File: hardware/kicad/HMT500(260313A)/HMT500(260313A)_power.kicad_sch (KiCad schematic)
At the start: 21 parts, among them U1 TPS26600PWPR, U2 LMR36006, U3 TPS7A2033PDBVR

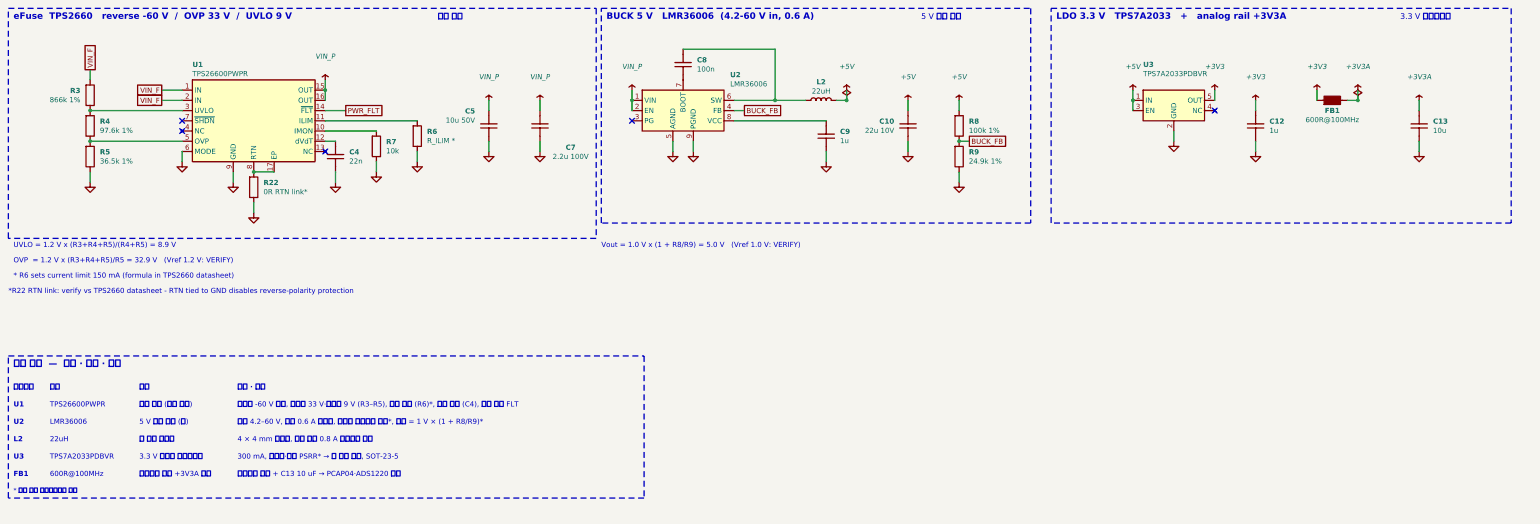
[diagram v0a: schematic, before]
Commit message: Schematic v0.8: apply datasheet review A-O (HMT500(260313A))
- Real pinouts from manufacturer datasheets: LMR36006BRNXR (RNX-12),
  TPS26611DDFR (SOT-23-8), PCAP04 (QFN24); TPS2660 PowerPAD = RTN
- TPS2660: RTN isolated from GND (R22, R7 removed); R5/R6/C4/MODE on
  EF_RTN; R6 80.6k (149 mA); R5 41.2k -> OVP 29 V, supply 12-28 V so
  TPS26611 +Vs stays <= 30 V
- DAC SPI: per-DAC SCLK gating (74LVC2G32, SPI2 mode 3, LATCH1/2 on
  PB10/PB11) - daisy chain was removed in DAC8760 rev D
- DAC AVDD 10R series, ALARM wired-OR with 10k pull-up (PB6)
- Output TVS -> TVS3301 (stacked-pin two-terminal symbol)
- PCAP04 on dedicated SPI3 (PB3/4/5), VDD18 4.7uF, VDD33 10uF
- Buck per datasheet: L 15uH, COUT 2x22uF, CFF 20pF
- Shared VIN_P bulk (C53, C26 removed); PWR_FLT PB7; SGOOD -> PC6/PC7
- Parts list, circuit-design, decision log #26, review doc updated;
  netlist 74/74, 0 errors; tests pass

Co-Authored-By: Claude Opus 5.5 <noreply@anthropic.com>
Claude-Session: https://claude.ai/code/session_01JA2o8uJsqp9Vzsg4b665ev
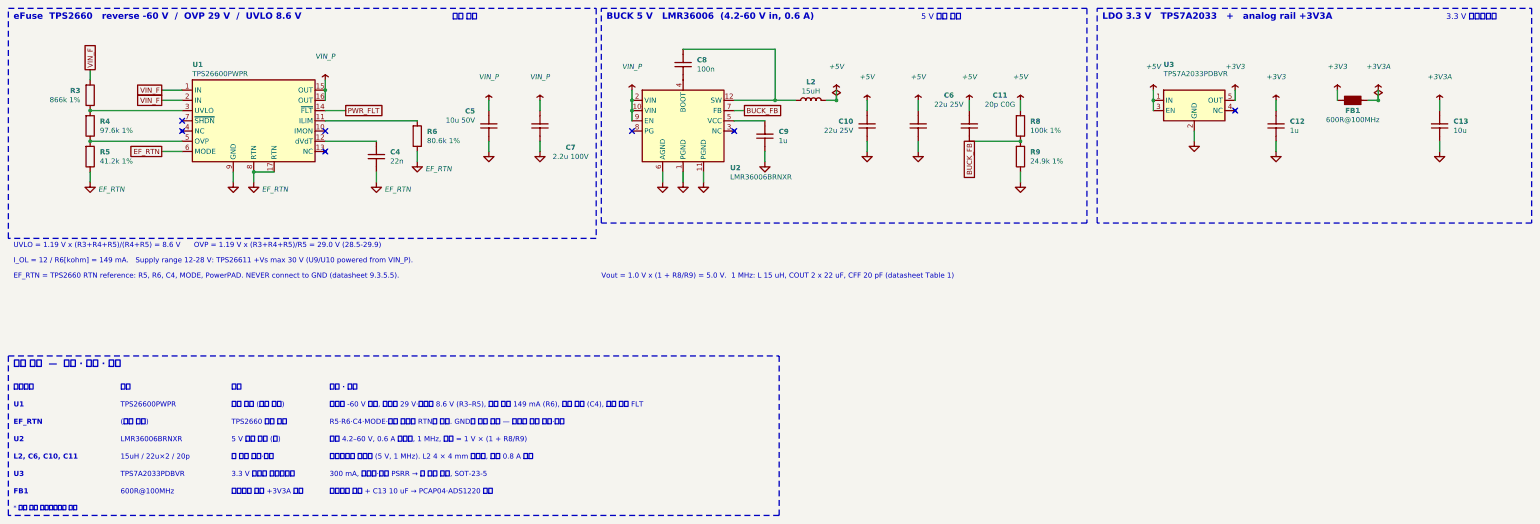
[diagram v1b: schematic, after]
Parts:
- removed R22: 0R RTN link*, Resistor_SMD:R_0603_1608Metric, symbol HMT500_260313A:R
- removed R7: 10k, Resistor_SMD:R_0603_1608Metric, symbol HMT500_260313A:R
- added C11: 20p C0G, Capacitor_SMD:C_0603_1608Metric, symbol HMT500_260313A:C
- added C6: 22u 25V, Capacitor_SMD:C_1206_3216Metric, symbol HMT500_260313A:C
- C10: value 22u 10V -> 22u 25V; footprint Capacitor_SMD:C_0805_2012Metric -> Capacitor_SMD:C_1206_3216Metric
- L2: value 22uH -> 15uH
- R5: value 36.5k 1% -> 41.2k 1%
- R6: value R_ILIM * -> 80.6k 1%
- U1: VERIFY YES - pin numbers are placeholders -> (none)
- U2: value LMR36006 -> LMR36006BRNXR; footprint TBD:VQFN-HR-12_LMR36006 -> TBD:Texas_RNX0012A_VQFN-HR-12_2x3mm; VERIFY YES - pin numbers are placeholders -> (none)
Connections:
- net +5V: now also C11.1, C6.1
- net BUCK_FB: now also U2.7 (FB), C11.2; no longer U2.4 (FB)
- net GND: now also U2.1 (PGND), U2.11 (PGND), U2.6 (AGND), C6.2; no longer C4.2, R5.2, R6.2, U1.6 (MODE), U2.5 (AGND), U2.9 (PGND)
- net VIN_P: now also U2.10 (VIN), U2.9 (EN); no longer U2.1 (VIN)
- net EF_RTN: now reaches U1.17 (RTN), U1.8 (RTN)
- net EF_RTN: now also C4.2, R5.2, R6.2, U1.6 (MODE)
- net at C8.1, L2.1: now also U2.12 (SW); no longer U2.6 (SW)
- net at C8.2: now also U2.4 (BOOT); no longer U2.7 (BOOT)
- net at C9.1: now also U2.5 (VCC); no longer U2.8 (VCC)
- no-connect marks 5 -> 7
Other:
- note added: "(기준 접지)"
- note added: "15uH / 22u×2 / 20p"
- note added: "300 mA, 저잡음·높은 PSRR → 벅 리플 제거, SOT-23-5"
- note added: "EF_RTN"
- note added: "EF_RTN = TPS2660 RTN reference: R5, R6, C4, MODE, PowerPAD. NEVER connect to GND (datasheet 9.3.5.5)."
- note added: "I_OL = 12 / R6[kohm] = 149 mA. Supply range 12-28 V: TPS26611 +Vs max 30 V (U9/U10 powered from VIN_P)."
- note added: "L2, C6, C10, C11"
- note added: "LMR36006BRNXR"
- note added: "R5·R6·C4·MODE·방열 패드는 RTN에 연결. GND와 연결 금지 — 역극성 보호 무효·손상"
- note added: "TPS2660 내부 기준"
- note added: "UVLO = 1.19 V x (R3+R4+R5)/(R4+R5) = 8.6 V OVP = 1.19 V x (R3+R4+R5)/R5 = 29.0 V (28.5-29.9)"
- note added: "Vout = 1.0 V x (1 + R8/R9) = 5.0 V. 1 MHz: L 15 uH, COUT 2 x 22 uF, CFF 20 pF (datasheet Table 1)"
- note added: "eFuse TPS2660 reverse -60 V / OVP 29 V / UVLO 8.6 V"
- note added: "데이터시트 권장값 (5 V, 1 MHz). L2 4 × 4 mm 차폐형, 포화 0.8 A 이상"
- note added: "벅 출력 필터·보상"
- note added: "역극성 -60 V 차단, 과전압 29 V·저전압 8.6 V (R3–R5), 전류 제한 149 mA (R6), 돌입 제한 (C4), 고장 출력 FLT"
- note added: "입력 4.2–60 V, 0.6 A 동기식, 1 MHz, 출력 = 1 V × (1 + R8/R9)"
- note removed: "* R6 sets current limit 150 mA (formula in TPS2660 datasheet)"
- note removed: "*R22 RTN link: verify vs TPS2660 datasheet - RTN tied to GND disables reverse-polarity protection"
- note removed: "22uH"
- note removed: "300 mA, 저잡음·높은 PSRR* → 벅 리플 제거, SOT-23-5"
- note removed: "4 × 4 mm 차폐형, 포화 전류 0.8 A 이상으로 선정"
- note removed: "L2"
- note removed: "LMR36006"
- note removed: "OVP = 1.2 V x (R3+R4+R5)/R5 = 32.9 V (Vref 1.2 V: VERIFY)"
- note removed: "UVLO = 1.2 V x (R3+R4+R5)/(R4+R5) = 8.9 V"
- note removed: "Vout = 1.0 V x (1 + R8/R9) = 5.0 V (Vref 1.0 V: VERIFY)"
- note removed: "eFuse TPS2660 reverse -60 V / OVP 33 V / UVLO 9 V"
- note removed: "벅 출력 인덕터"
- note removed: "역극성 -60 V 차단, 과전압 33 V·저전압 9 V (R3–R5), 전류 제한 (R6)*, 돌입 제한 (C4), 고장 출력 FLT"
- note removed: "입력 4.2–60 V, 출력 0.6 A 동기식, 무부하 소비전류 작음*, 출력 = 1 V × (1 + R8/R9)*"
- moved on the sheet: C10, C12, C13, C4, C9, FB1, L2, R8, R9, U3

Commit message: Schematic: global label shape shows signal direction (driver = output, receiver = input)
Direction derived per net from pin types (output / tri-state / open-drain
drivers, MCU as driver when only inputs are on the other side); analog
and passive nets keep the plain shape, RS-485 bus bidirectional.
Legend line on the root sheet; test for key nets.

Co-Authored-By: Claude Opus 5.5 <noreply@anthropic.com>
Claude-Session: https://claude.ai/code/session_01JA2o8uJsqp9Vzsg4b665ev
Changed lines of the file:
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@@
 (global_label "VIN_F" (shape passive) (at 45.72 81.28 90) (fields_autoplaced) (effects (font (size 1.27 1.27)) (justify left)) (property "Intersheetrefs" "${INTERSHEET_REFS}" (at 45.72 81.28 0) (effects (font (size 1.27 1.27)) hide)))
 (global_label "EF_RTN" (shape passive) (at 63.5 101.6 180) (fields_autoplaced) (effects (font (size 1.27 1.27)) (justify right)) (property "Intersheetrefs" "${INTERSHEET_REFS}" (at 63.5 101.6 0) (effects (font (size 1.27 1.27)) hide)))
-(global_label "PWR_FLT" (shape passive) (at 109.22 91.44 0) (fields_autoplaced) (effects (font (size 1.27 1.27)) (justify left)) (property "Intersheetrefs" "${INTERSHEET_REFS}" (at 109.22 91.44 0) (effects (font (size 1.27 1.27)) hide)))
+(global_label "PWR_FLT" (shape output) (at 109.22 91.44 0) (fields_autoplaced) (effects (font (size 1.27 1.27)) (justify left)) (property "Intersheetrefs" "${INTERSHEET_REFS}" (at 109.22 91.44 0) (effects (font (size 1.27 1.27)) hide)))
 (global_label "BUCK_FB" (shape passive) (at 208.28 91.44 0) (fields_autoplaced) (effects (font (size 1.27 1.27)) (justify left)) (property "Intersheetrefs" "${INTERSHEET_REFS}" (at 208.28 91.44 0) (effects (font (size 1.27 1.27)) hide)))
 (global_label "BUCK_FB" (shape passive) (at 264.16 99.06 270) (fields_autoplaced) (effects (font (size 1.27 1.27)) (justify right)) (property "Intersheetrefs" "${INTERSHEET_REFS}" (at 264.16 99.06 0) (effects (font (size 1.27 1.27)) hide)))

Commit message: Schematic: wire nearby same-sheet nets, signal-flow direction for analog nets
- Analog: +VSENSE and terminal feedback drawn as wires to the OPA197
  buffer (no DACn_SENSE / second OUTn_EXT labels); U14 1A/2A tied, one
  DAC_SCK label
- Power: TPS2660 left pins reordered so R3-R5 run straight from IN to
  UVLO/OVP; one VIN_F label
- Measurement: C27 sits directly between R17/R18 and AIN1/AIN2
- MCU: SWD pads (J2) placed on the PA13/PA14 rows and wired directly
- Label direction for passive nets from signal flow: OUTn_EXT analog ->
  connector, VIN_F connector -> eFuse, BUCK_FB divider -> FB
- Tests: nearby same-sheet labels must be wired; bend limit 6/sheet;
  check_netlist accepts KiCad auto-named multi-pin nets

Co-Authored-By: Claude Opus 5.5 <noreply@anthropic.com>
Claude-Session: https://claude.ai/code/session_01JA2o8uJsqp9Vzsg4b665ev
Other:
- moved on the sheet: R3, R4, R5

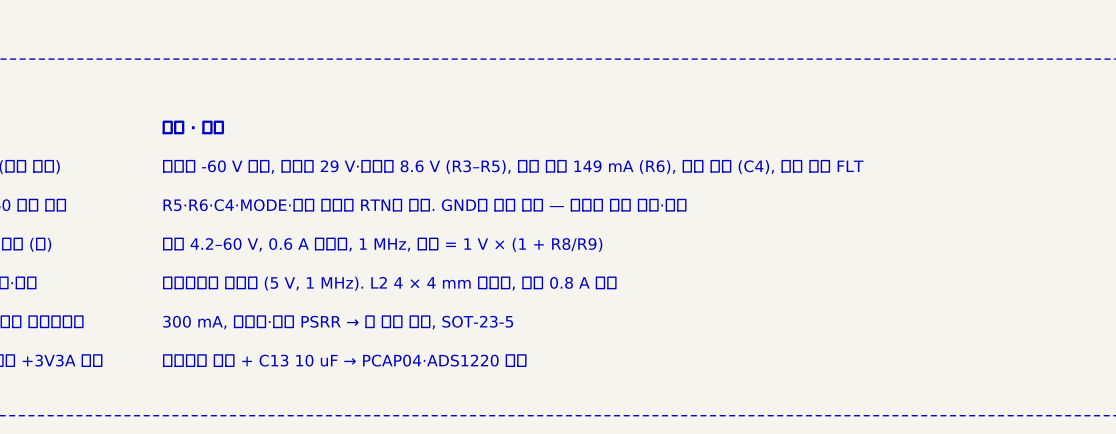
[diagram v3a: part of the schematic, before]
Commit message: Footprints and part numbers: no TBD left in the schematic
- Project footprint library hardware/kicad/lib/HMT500_260313A.pretty:
  KiCad 7.0.11 footprints + gen_footprints.py (LMR36006 RNX0012A from TI
  land pattern, Bourns 2035-xx-SM GDT, TVS3301 DRB with floating pad)
- GDT changed to 2-electrode Bourns 2035-23-SM-RPLF (2038 is 3-electrode)
- L1 Wurth WE-SL2 744222 (1 mH, 0.8 A); CMC pins renumbered to WE-SL2
  windings 1-4 / 2-3
- J5 Harwin S1941-46R, L2 Coilcraft XGL4030-153MEC, TPS26611 SOT-23-8,
  TPS2660 HTSSOP-16 footprint from 7.0.11
- R1 MMB02070C4708FB200, R30/R40 CRCW251210R0FKEGHP confirmed;
  R19 -> Vishay PLTT0603 0.02 % 5 ppm
- fp-lib-table written by the generator; netlist 74/74, tests pass

Co-Authored-By: Claude Opus 5.5 <noreply@anthropic.com>
Claude-Session: https://claude.ai/code/session_01JA2o8uJsqp9Vzsg4b665ev
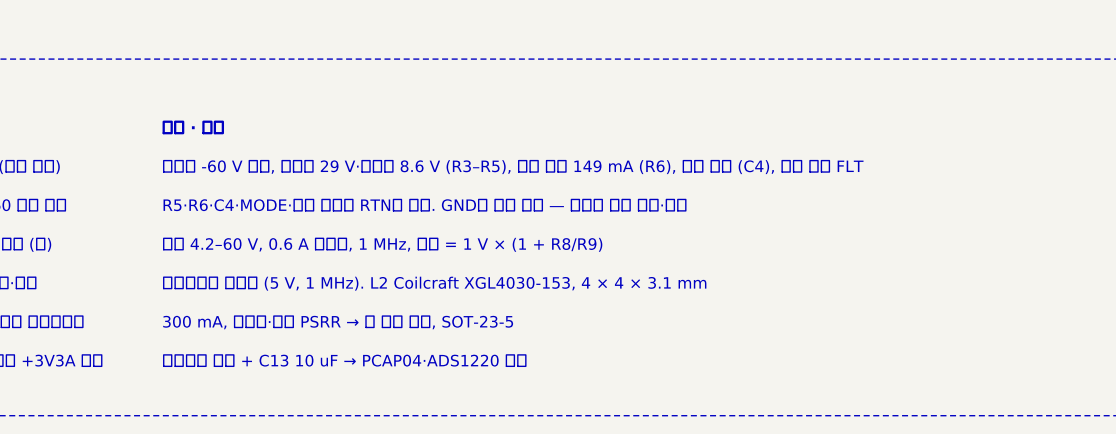
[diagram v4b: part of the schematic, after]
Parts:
- L2: footprint TBD:L_4x4mm -> Inductor_SMD:L_Coilcraft_XAL4030-XXX
- U1: footprint Package_SO:HTSSOP-16-1EP_4.4x5mm_P0.65mm_EP3.4x5mm_Mask2.66x2.46mm_ThermalVias -> Package_SO:HTSSOP-16-1EP_4.4x5mm_P0.65mm_EP3.4x5mm_Mask2.46x2.31mm_ThermalVias
- U2: footprint TBD:Texas_RNX0012A_VQFN-HR-12_2x3mm -> HMT500_260313A:Texas_RNX0012A_VQFN-HR-12_2x3mm
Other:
- note added: "데이터시트 권장값 (5 V, 1 MHz). L2 Coilcraft XGL4030-153, 4 × 4 × 3.1 mm"
- note removed: "데이터시트 권장값 (5 V, 1 MHz). L2 4 × 4 mm 차폐형, 포화 0.8 A 이상"

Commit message: Schematic v0.9 + placement rev 4: apply triple-review A/B items, re-review fixes
- Power: OVP 32.6 V (R5 36.5k), D2 TVS3301, C2 2.2u 100V, buck input 220n x2,
  U2 pin 3 = SW; TPS26611 +Vs emitter-follower clamp (Q1 MMBTA06, R50, D50 27V)
- RS-485: THVD2410, DE 10k pull-down (R60) for in-house bootloader
- MCU: SGOOD on PA0/PA4, CS_CDC PA15, VIN_SENSE PB0, LATCH/CS pull-ups,
  SWD no-connect removed, netlist checker flags no-connect on used pins
- Analog: OPA197 V+ = DAC AVDD, R31/R41 100k, local caps; X7R throughout
- New aux sheet; SOT-23 and R1206 footprints; parts list and JLC files
- Placement: pin-targeted hints, MCU decaps under U4, chassis parts grouped
  in front, J5 keep-out 3.3 mm, CHASSIS netclass; 102/102 parts placed
- Docs: final review H table, decision #32, circuit design, placement rev 4

Co-Authored-By: Claude Opus 5.5 <noreply@anthropic.com>
Claude-Session: https://claude.ai/code/session_01JA2o8uJsqp9Vzsg4b665ev
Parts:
- added C16, C17: 220n 100V, Capacitor_SMD:C_0603_1608Metric, symbol HMT500_260313A:C
- added C2: 2.2u 100V, Capacitor_SMD:C_1210_3225Metric, symbol HMT500_260313A:C
- added C26: 1u, Capacitor_SMD:C_0603_1608Metric, symbol HMT500_260313A:C
- C13: footprint Capacitor_SMD:C_0805_2012Metric -> Capacitor_SMD:C_1206_3216Metric
- R5: value 41.2k 1% -> 36.5k 1%
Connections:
- net +5V: now also C26.1
- net GND: now also C16.2, C17.2, C2.2, C26.2
- net VIN_F: now also C2.1
- net VIN_P: now also C16.1, C17.1
- net BUCK_SW: now reaches C8.1, L2.1, U2.12 (SW)
- net BUCK_SW: now also U2.3 (NC(SW))
- no-connect marks 7 -> 6
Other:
- note added: "2.2u 100V"
- note added: "220n ×2 (+10u)"
- note added: "C16, C17 (+C5)"
- note added: "C16/C17 at U2 VIN-PGND, C5 (bulk) next to U2; C26 at U3 IN"
- note added: "C2"
- note added: "I_OL = 12 / R6 = 149 mA. Supply 12-28 V recovers after OVP trip (fall > 29.2 V). TPS26611 +Vs clamped (sheet Aux)."
- note added: "LOCAL INPUT CAPS"
- note added: "TVS와 함께 IN ≥ 1 uF (데이터시트 11.1), U1 핀 옆 — 핫플러그 링잉 억제"
- note added: "UVLO = 1.19 V x (R3+R4+R5)/(R4+R5) = 8.9 V OVP rise 1.19 V x (R3+R4+R5)/R5 = 32.6 V (31.5-34.2), fall 30.1 V"
- note added: "VIN–PGND 핀마다 220 nF, 벌크 C5 10 uF를 U2 옆에 (데이터시트 CIN 4.7 uF + 220 nF × 2)"
- note added: "eFuse TPS2660 reverse -60 V / OVP 32.6 V / UVLO 8.9 V"
- note added: "eFuse 입력 콘덴서"
- note added: "국부 입력 콘덴서"
- note added: "벅 입력 콘덴서"
- note added: "역극성 -60 V 차단, 과전압 32.6 V (복귀 30.1 V)·저전압 8.9 V (R3–R5), 전류 제한 149 mA (R6), 돌입 제한 (C4), 고장 출력 FLT"
- note removed: "I_OL = 12 / R6[kohm] = 149 mA. Supply range 12-28 V: TPS26611 +Vs max 30 V (U9/U10 powered from VIN_P)."
- note removed: "UVLO = 1.19 V x (R3+R4+R5)/(R4+R5) = 8.6 V OVP = 1.19 V x (R3+R4+R5)/R5 = 29.0 V (28.5-29.9)"
- note removed: "eFuse TPS2660 reverse -60 V / OVP 29 V / UVLO 8.6 V"
- note removed: "역극성 -60 V 차단, 과전압 29 V·저전압 8.6 V (R3–R5), 전류 제한 149 mA (R6), 돌입 제한 (C4), 고장 출력 FLT"

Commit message: Map BOM to JLCPCB/LCSC parts (decision #34) and re-place
- 50 of 55 BOM lines have LCSC numbers (make_parts_list.LCSC); parts list
  gets LCSC / JLC class columns; JLC BOM and harness order filled
- Keep MCU (125 C grade), LMR36006, R19 precision ref and pulse resistors
  via JLC global sourcing
- LCSC-driven footprint changes: C6/C10 1210, C16/C17 0805, R1 2512,
  L2 XAL4040; C3 2 kV X7R 1812, GDT 2035-25, L1 SRF0905 (to verify)
- Re-placed: 102/102, netlist 77/77, assembly sim 23 OK

Co-Authored-By: Claude Opus 5.5 <noreply@anthropic.com>
Claude-Session: https://claude.ai/code/session_01JA2o8uJsqp9Vzsg4b665ev
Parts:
- C10, C6: footprint Capacitor_SMD:C_1206_3216Metric -> Capacitor_SMD:C_1210_3225Metric
- C16, C17: footprint Capacitor_SMD:C_0603_1608Metric -> Capacitor_SMD:C_0805_2012Metric
- L2: footprint Inductor_SMD:L_Coilcraft_XAL4030-XXX -> Inductor_SMD:L_Coilcraft_XAL4040-XXX

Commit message: Apply agreed external review items (decision #35)
- H01: series 100 V Schottky D3 (PMEG10010ELR) between D2 and eFuse IN
  (new net VIN_D) so negative surges no longer stress U1 IN-OUT
- H02: RS-485 bus TVS D60/D61 (TVS3301); U11 -> THVD2410DGKR (VSSOP-8)
- H04: +Vs clamp zener 27 V -> 24 V (BZX84C24LT1G)
- H08: ADS1220 IDAC fixed at 250 uA
- Room for new parts: C7 removed, 37 low-voltage R/C moved to 0402
  (LCSC basic where available); chassis parts keep CH_GAP between each other
- Placement 104/104, netlist 78/78, pcbnew DRC: no clearance errors,
  assembly sim 23 OK; parts list / JLC BOM updated
- docs/hw/external-review-response-260930.md: item responses, output load
  table, current budget, firmware requirements F1-F6, tests T1-T7

Co-Authored-By: Claude Opus 5.5 <noreply@anthropic.com>
Claude-Session: https://claude.ai/code/session_01JA2o8uJsqp9Vzsg4b665ev
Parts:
- removed C7: 2.2u 100V, Capacitor_SMD:C_1210_3225Metric, symbol HMT500_260313A:C
- C11, C12, C26, C4, C8, C9: footprint Capacitor_SMD:C_0603_1608Metric -> Capacitor_SMD:C_0402_1005Metric
- R8: footprint Resistor_SMD:R_0603_1608Metric -> Resistor_SMD:R_0402_1005Metric
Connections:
- net VIN_F renamed VIN_D
